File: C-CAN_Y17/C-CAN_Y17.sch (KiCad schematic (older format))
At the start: 10 parts

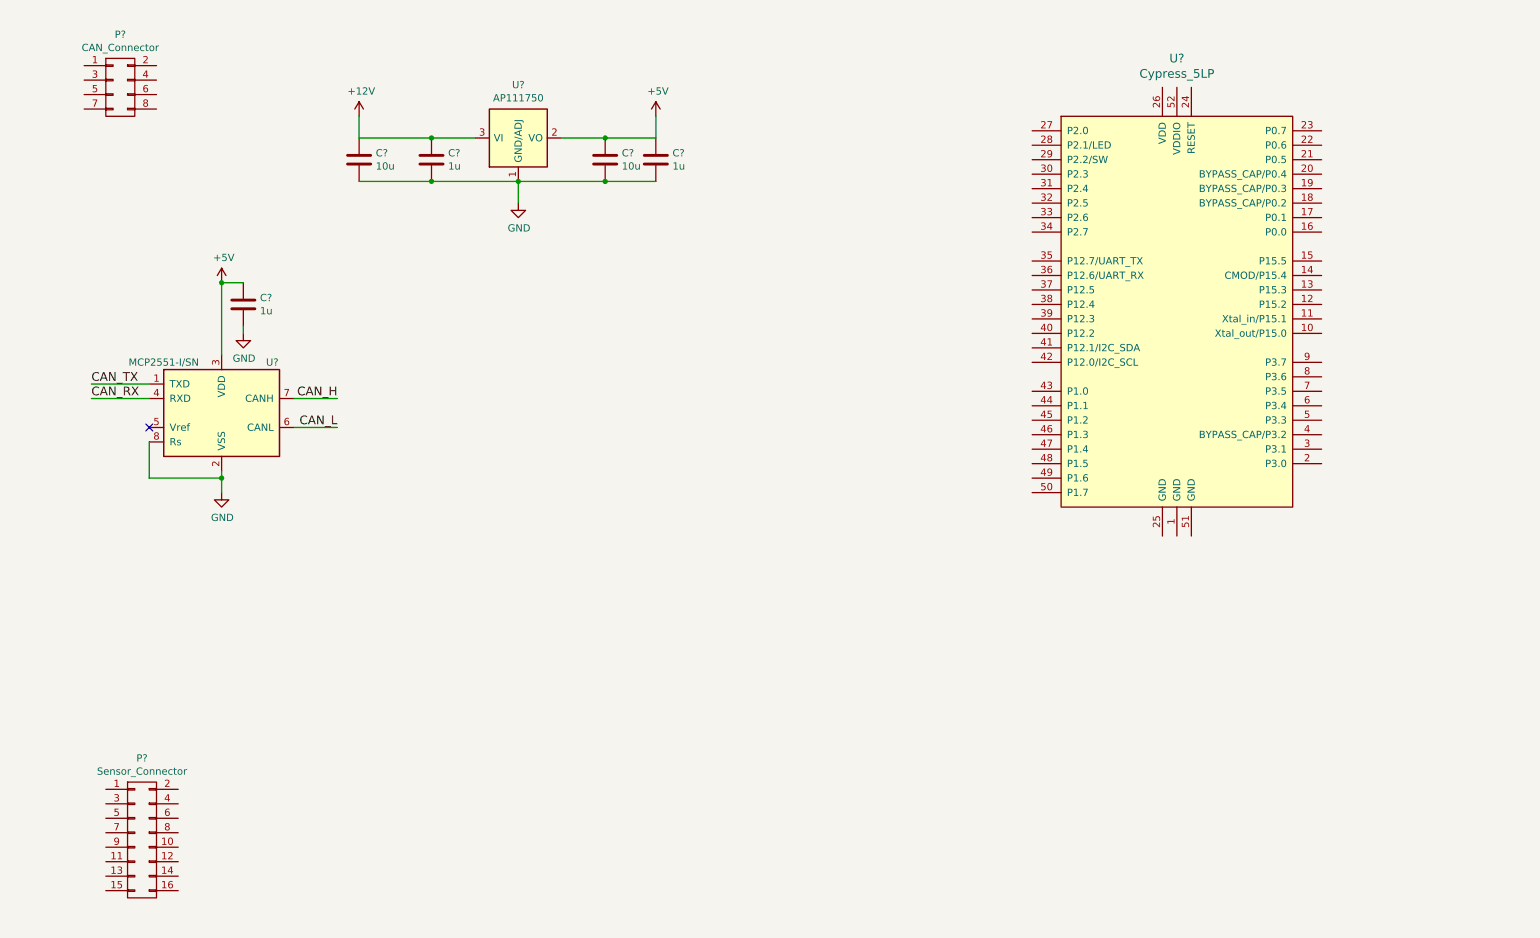
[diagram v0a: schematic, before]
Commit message: More work on new C-CAN
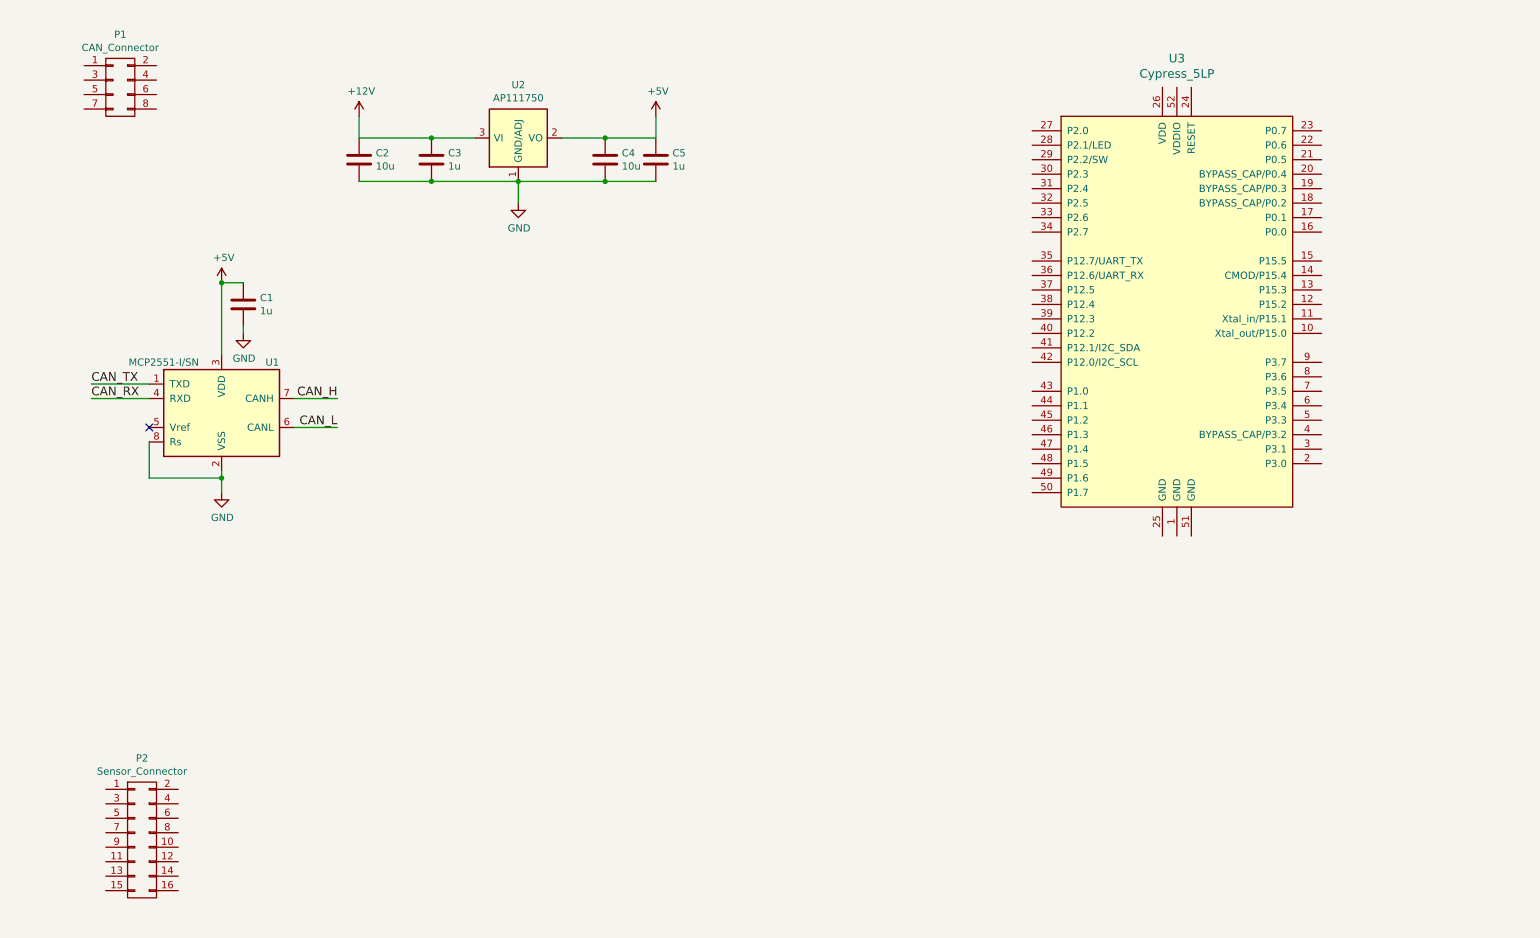
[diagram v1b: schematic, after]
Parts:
- P2: renamed from P?; footprint (none) -> UNCAMotorsports:MX150_16pin
- gave numbers to parts that had none: 9
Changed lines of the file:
@@
 LIBS:contrib
 LIBS:valves
+LIBS:Cypress_cy8c5xlp
 LIBS:UNCAMotorsports
-LIBS:Cypress_cy8c5xlp
+LIBS:relays
+LIBS:SystemBlocks
+LIBS:C-CAN_Y17-cache
 EELAYER 26 0
 EELAYER END
@@
 $EndDescr
 $Comp
-L Cypress_5LP U?
+L Cypress_5LP U3
 U 1 1 58B77315
 P 8800 2600
-F 0 "U?" H 8800 4300 60  0000 C CNN
+F 0 "U3" H 8800 4300 60  0000 C CNN
 F 1 "Cypress_5LP" H 8800 4194 60  0000 C CNN
-F 2 "" H 8800 2800 60  0000 C CNN
+F 2 "" H 8800 2800 60  0001 C CNN
 F 3 "" H 8800 2800 60  0000 C CNN
 	1    8800 2600
@@
 $EndComp
 $Comp
-L MCP2551-I/SN U?
+L MCP2551-I/SN U1
 U 1 1 58B7735B
 P 2200 3350
-F 0 "U?" H 2550 3700 50  0000 C CNN
+F 0 "U1" H 2550 3700 50  0000 C CNN
 F 1 "MCP2551-I/SN" H 1800 3700 50  0000 C CNN
 F 2 "Housings_SOIC:SOIC-8_3.9x4.9mm_Pitch1.27mm" H 2200 2850 50  0001 C CIN
@@
 $EndComp
 $Comp
-L AP111750 U?
+L AP111750 U2
 U 1 1 58B7742F
 P 4250 1450
-F 0 "U?" H 4250 1817 50  0000 C CNN
+F 0 "U2" H 4250 1817 50  0000 C CNN
 F 1 "AP111750" H 4250 1726 50  0000 C CNN
 F 2 "TO_SOT_Packages_SMD:SOT-223" H 4250 1100 50  0001 C CNN
@@
 $EndComp
 $Comp
-L CONN_02X04 P?
+L CONN_02X04 P1
 U 1 1 58B775B9
 P 1500 1100
-F 0 "P?" H 1500 1465 50  0000 C CNN
+F 0 "P1" H 1500 1465 50  0000 C CNN
 F 1 "CAN_Connector" H 1500 1374 50  0000 C CNN
-F 2 "" H 1500 -100 50  0000 C CNN
+F 2 "" H 1500 -100 50  0001 C CNN
 F 3 "" H 1500 -100 50  0000 C CNN
 	1    1500 1100
@@
 $EndComp
 $Comp
-L CONN_02X08 P?
+L CONN_02X08 P2
 U 1 1 58B77DCE
 P 1650 6300
-F 0 "P?" H 1650 6865 50  0000 C CNN
+F 0 "P2" H 1650 6865 50  0000 C CNN
 F 1 "Sensor_Connector" H 1650 6774 50  0000 C CNN
-F 2 "" H 1650 5100 50  0000 C CNN
+F 2 "UNCAMotorsports:MX150_16pin" H 1650 5100 50  0001 C CNN
 F 3 "" H 1650 5100 50  0000 C CNN
 	1    1650 6300
@@
 $EndComp
 $Comp
-L +12V #PWR?
+L +12V #PWR01
 U 1 1 58B77F9E
 P 3150 1300
-F 0 "#PWR?" H 3150 1150 50  0001 C CNN
+F 0 "#PWR01" H 3150 1150 50  0001 C CNN
 F 1 "+12V" H 3165 1473 50  0000 C CNN
 F 2 "" H 3150 1300 50  0000 C CNN
@@
 $EndComp
 $Comp
-L +5V #PWR?
+L +5V #PWR02
 U 1 1 58B77FBC
 P 5200 1300
-F 0 "#PWR?" H 5200 1150 50  0001 C CNN
+F 0 "#PWR02" H 5200 1150 50  0001 C CNN
 F 1 "+5V" H 5215 1473 50  0000 C CNN
 F 2 "" H 5200 1300 50  0000 C CNN
@@
 $EndComp
 $Comp
-L C C?
+L C C2
 U 1 1 58B77FDA
 P 3150 1600
-F 0 "C?" H 3265 1646 50  0000 L CNN
+F 0 "C2" H 3265 1646 50  0000 L CNN
 F 1 "10u" H 3265 1555 50  0000 L CNN
-F 2 "" H 3188 1450 50  0000 C CNN
+F 2 "" H 3188 1450 50  0001 C CNN
 F 3 "" H 3150 1600 50  0000 C CNN
 	1    3150 1600
@@
 $EndComp
 $Comp
-L C C?
+L C C3
 U 1 1 58B78024
 P 3650 1600
-F 0 "C?" H 3765 1646 50  0000 L CNN
+F 0 "C3" H 3765 1646 50  0000 L CNN
 F 1 "1u" H 3765 1555 50  0000 L CNN
-F 2 "" H 3688 1450 50  0000 C CNN
+F 2 "" H 3688 1450 50  0001 C CNN
 F 3 "" H 3650 1600 50  0000 C CNN
 	1    3650 1600
@@
 $EndComp
 $Comp
-L C C?
+L C C4
 U 1 1 58B7804C
 P 4850 1600
-F 0 "C?" H 4965 1646 50  0000 L CNN
+F 0 "C4" H 4965 1646 50  0000 L CNN
 F 1 "10u" H 4965 1555 50  0000 L CNN
-F 2 "" H 4888 1450 50  0000 C CNN
+F 2 "" H 4888 1450 50  0001 C CNN
 F 3 "" H 4850 1600 50  0000 C CNN
 	1    4850 1600
@@
 $EndComp
 $Comp
-L C C?
+L C C5
 U 1 1 58B7807E
 P 5200 1600
-F 0 "C?" H 5315 1646 50  0000 L CNN
+F 0 "C5" H 5315 1646 50  0000 L CNN
 F 1 "1u" H 5315 1555 50  0000 L CNN
-F 2 "" H 5238 1450 50  0000 C CNN
+F 2 "" H 5238 1450 50  0001 C CNN
 F 3 "" H 5200 1600 50  0000 C CNN
 	1    5200 1600
@@
 	5200 1450 5200 1300
 $Comp
-L GND #PWR?
+L GND #PWR03
 U 1 1 58B78147
 P 4250 1900
-F 0 "#PWR?" H 4250 1650 50  0001 C CNN
+F 0 "#PWR03" H 4250 1650 50  0001 C CNN
 F 1 "GND" H 4255 1727 50  0000 C CNN
 F 2 "" H 4250 1900 50  0000 C CNN
@@
 Connection ~ 4850 1750
 $Comp
-L GND #PWR?
+L GND #PWR04
 U 1 1 58B78482
 P 2200 3900
-F 0 "#PWR?" H 2200 3650 50  0001 C CNN
+F 0 "#PWR04" H 2200 3650 50  0001 C CNN
 F 1 "GND" H 2205 3727 50  0000 C CNN
 F 2 "" H 2200 3900 50  0000 C CNN
@@
 	2700 3450 3000 3450
 $Comp
-L +5V #PWR?
+L +5V #PWR05
 U 1 1 58B786DB
 P 2200 2450
-F 0 "#PWR?" H 2200 2300 50  0001 C CNN
+F 0 "#PWR05" H 2200 2300 50  0001 C CNN
 F 1 "+5V" H 2215 2623 50  0000 C CNN
 F 2 "" H 2200 2450 50  0000 C CNN
@@
 	2200 2450 2200 2950
 $Comp
-L C C?
+L C C1
 U 1 1 58B78755
 P 2350 2600
-F 0 "C?" H 2465 2646 50  0000 L CNN
+F 0 "C1" H 2465 2646 50  0000 L CNN
 F 1 "1u" H 2465 2555 50  0000 L CNN
-F 2 "" H 2388 2450 50  0000 C CNN
+F 2 "" H 2388 2450 50  0001 C CNN
 F 3 "" H 2350 2600 50  0000 C CNN
 	1    2350 2600
@@
 $EndComp
 $Comp
-L GND #PWR?
+L GND #PWR06
 U 1 1 58B7879B
 P 2350 2800
-F 0 "#PWR?" H 2350 2550 50  0001 C CNN
+F 0 "#PWR06" H 2350 2550 50  0001 C CNN
 F 1 "GND" H 2355 2627 50  0000 C CNN
 F 2 "" H 2350 2800 50  0000 C CNN

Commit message: "        "
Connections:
- net +12V: now also P1.1 (P1), P1.4 (P4)
- net +5V: now also P2.1 (P1), P2.4 (P4), P2.7 (P7), P2.9 (P9)
- net CAN_H: now also P1.2 (P2), P1.3 (P3)
- net CAN_L: now also P1.6 (P6), P1.7 (P7)
- net GND: now also P1.5 (P5), P1.8 (P8), P2.3 (P3), P2.6 (P6)
- net S1: now reaches P2.2 (P2)
- net S2: now reaches P2.5 (P5)
- net H1: now reaches P2.8 (P8)
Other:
- moved on the sheet: P2
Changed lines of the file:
@@
 U 1 1 58B77315
 P 8800 2600
-F 0 "U3" H 8800 4300 60  0000 C CNN
-F 1 "Cypress_5LP" H 8800 4194 60  0000 C CNN
+F 0 "U3" H 8250 4050 60  0000 C CNN
+F 1 "Cypress_5LP" H 8300 3950 60  0000 C CNN
 F 2 "" H 8800 2800 60  0001 C CNN
 F 3 "" H 8800 2800 60  0000 C CNN
@@
 L CONN_02X08 P2
 U 1 1 58B77DCE
-P 1650 6300
-F 0 "P2" H 1650 6865 50  0000 C CNN
-F 1 "Sensor_Connector" H 1650 6774 50  0000 C CNN
-F 2 "UNCAMotorsports:MX150_16pin" H 1650 5100 50  0001 C CNN
-F 3 "" H 1650 5100 50  0000 C CNN
-	1    1650 6300
+P 3400 5350
+F 0 "P2" H 3400 5915 50  0000 C CNN
+F 1 "Sensor_Connector" H 3400 5824 50  0000 C CNN
+F 2 "UNCAMotorsports:MX150_16pin" H 3400 4150 50  0001 C CNN
+F 3 "" H 3400 4150 50  0000 C CNN
+	1    3400 5350
 	1    0    0    -1
 $EndComp
@@
 	2350 2450 2200 2450
 Connection ~ 2200 2450
+Text Label 950  1050 0    60   ~ 0
+CAN_H
+Text Label 2100 950  2    60   ~ 0
+CAN_H
+Wire Wire Line
+	2100 950  1750 950
+$Comp
+L +12V #PWR?
+U 1 1 58B7A343
+P 850 950
+F 0 "#PWR?" H 850 800 50  0001 C CNN
+F 1 "+12V" H 865 1123 50  0000 C CNN
+F 2 "" H 850 950 50  0000 C CNN
+F 3 "" H 850 950 50  0000 C CNN
+	1    850  950
+	1    0    0    -1
+$EndComp
+Wire Wire Line
+	850  950  1250 950
+$Comp
+L +12V #PWR?
+U 1 1 58B7A390
+P 2200 1050
+F 0 "#PWR?" H 2200 900 50  0001 C CNN
+F 1 "+12V" H 2215 1223 50  0000 C CNN
+F 2 "" H 2200 1050 50  0000 C CNN
+F 3 "" H 2200 1050 50  0000 C CNN
+	1    2200 1050
+	1    0    0    -1
+$EndComp
+Wire Wire Line
+	2200 1050 1750 1050
+$Comp
+L GND #PWR?
+U 1 1 58B7A3DE
+P 850 1150
+F 0 "#PWR?" H 850 900 50  0001 C CNN
+F 1 "GND" H 855 977 50  0000 C CNN
+F 2 "" H 850 1150 50  0000 C CNN
+F 3 "" H 850 1150 50  0000 C CNN
+	1    850  1150
+	1    0    0    -1
+$EndComp
+Wire Wire Line
+	850  1150 1250 1150
+$Comp
+L GND #PWR?
+U 1 1 58B7A438
+P 2200 1250
+F 0 "#PWR?" H 2200 1000 50  0001 C CNN
+F 1 "GND" H 2205 1077 50  0000 C CNN
+F 2 "" H 2200 1250 50  0000 C CNN
+F 3 "" H 2200 1250 50  0000 C CNN
+	1    2200 1250
+	1    0    0    -1
+$EndComp
+Wire Wire Line
+	2200 1250 1750 1250
+Text Label 2100 1150 2    60   ~ 0
+CAN_L
+Wire Wire Line
+	2100 1150 1750 1150
+Text Label 950  1250 0    60   ~ 0
+CAN_L
+Wire Wire Line
+	950  1250 1250 1250
+Wire Wire Line
+	950  1050 1250 1050
+$Comp
+L +5V #PWR?
+U 1 1 58B7AF23
+P 2700 5000
+F 0 "#PWR?" H 2700 4850 50  0001 C CNN
+F 1 "+5V" H 2715 5173 50  0000 C CNN
+F 2 "" H 2700 5000 50  0000 C CNN
+F 3 "" H 2700 5000 50  0000 C CNN
+	1    2700 5000
+	1    0    0    -1
+$EndComp
+Wire Wire Line
+	2700 5000 3150 5000
+Text Label 3900 5000 2    60   ~ 0
+S1
+Wire Wire Line
+	3900 5000 3650 5000
+$Comp
+L GND #PWR?
+U 1 1 58B7B062
+P 2700 5100
+F 0 "#PWR?" H 2700 4850 50  0001 C CNN
+F 1 "GND" H 2705 4927 50  0000 C CNN
+F 2 "" H 2700 5100 50  0000 C CNN
+F 3 "" H 2700 5100 50  0000 C CNN
+	1    2700 5100
+	1    0    0    -1
+$EndComp
+Wire Wire Line
+	2700 5100 3150 5100
+$Comp
+L +5V #PWR?
+U 1 1 58B7B0B7
+P 4200 5100
+F 0 "#PWR?" H 4200 4950 50  0001 C CNN
+F 1 "+5V" H 4215 5273 50  0000 C CNN
+F 2 "" H 4200 5100 50  0000 C CNN
+F 3 "" H 4200 5100 50  0000 C CNN
+	1    4200 5100
+	1    0    0    -1
+$EndComp
+Wire Wire Line
+	4200 5100 3650 5100
+Text Label 3000 5200 0    60   ~ 0
+S2
+Wire Wire Line
+	3000 5200 3150 5200
+$Comp
+L GND #PWR?
+U 1 1 58B7B15B
+P 4200 5200
+F 0 "#PWR?" H 4200 4950 50  0001 C CNN
+F 1 "GND" H 4205 5027 50  0000 C CNN
+F 2 "" H 4200 5200 50  0000 C CNN
+F 3 "" H 4200 5200 50  0000 C CNN
+	1    4200 5200
+	1    0    0    -1
+$EndComp
+Wire Wire Line
+	4200 5200 3650 5200
+$Comp
+L +5V #PWR?
+U 1 1 58B7B1B3
+P 2500 5300
+F 0 "#PWR?" H 2500 5150 50  0001 C CNN
+F 1 "+5V" H 2515 5473 50  0000 C CNN
+F 2 "" H 2500 5300 50  0000 C CNN
+F 3 "" H 2500 5300 50  0000 C CNN
+	1    2500 5300
+	1    0    0    -1
+$EndComp
+Wire Wire Line
+	2500 5300 3150 5300
+Text Label 3900 5300 2    60   ~ 0
+H1
+Wire Wire Line
+	3900 5300 3650 5300
+Wire Wire Line
+	3150 5400 2500 5400
+Wire Wire Line
+	2500 5400 2500 5300
+Connection ~ 2500 5300
 $EndSCHEMATC

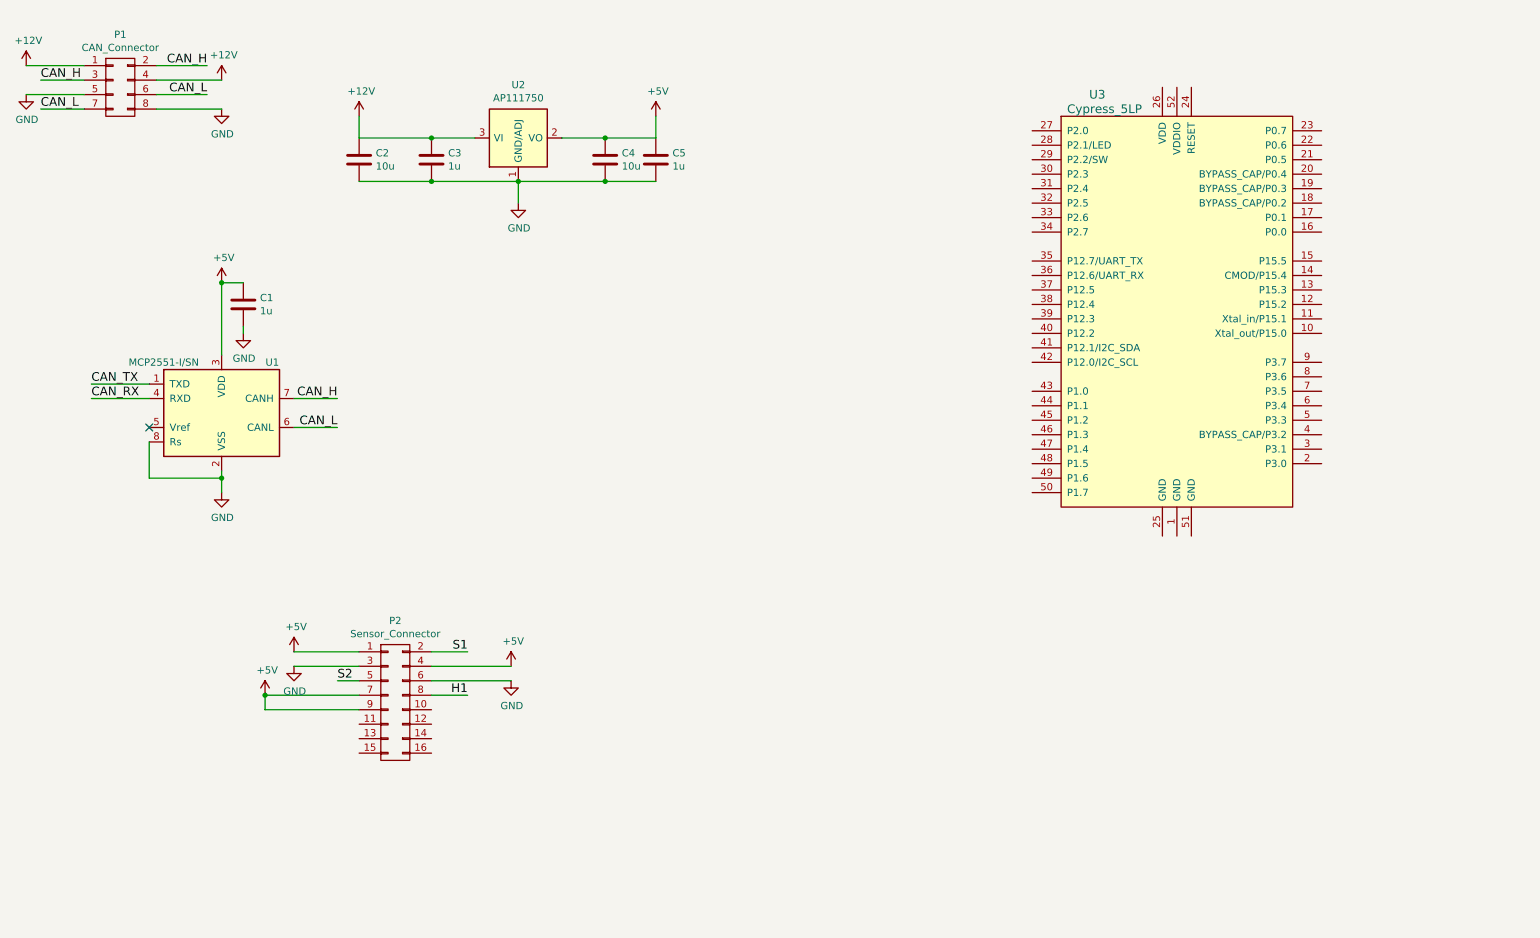
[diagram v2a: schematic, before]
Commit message: C-CAN_Y17 done except for pcb
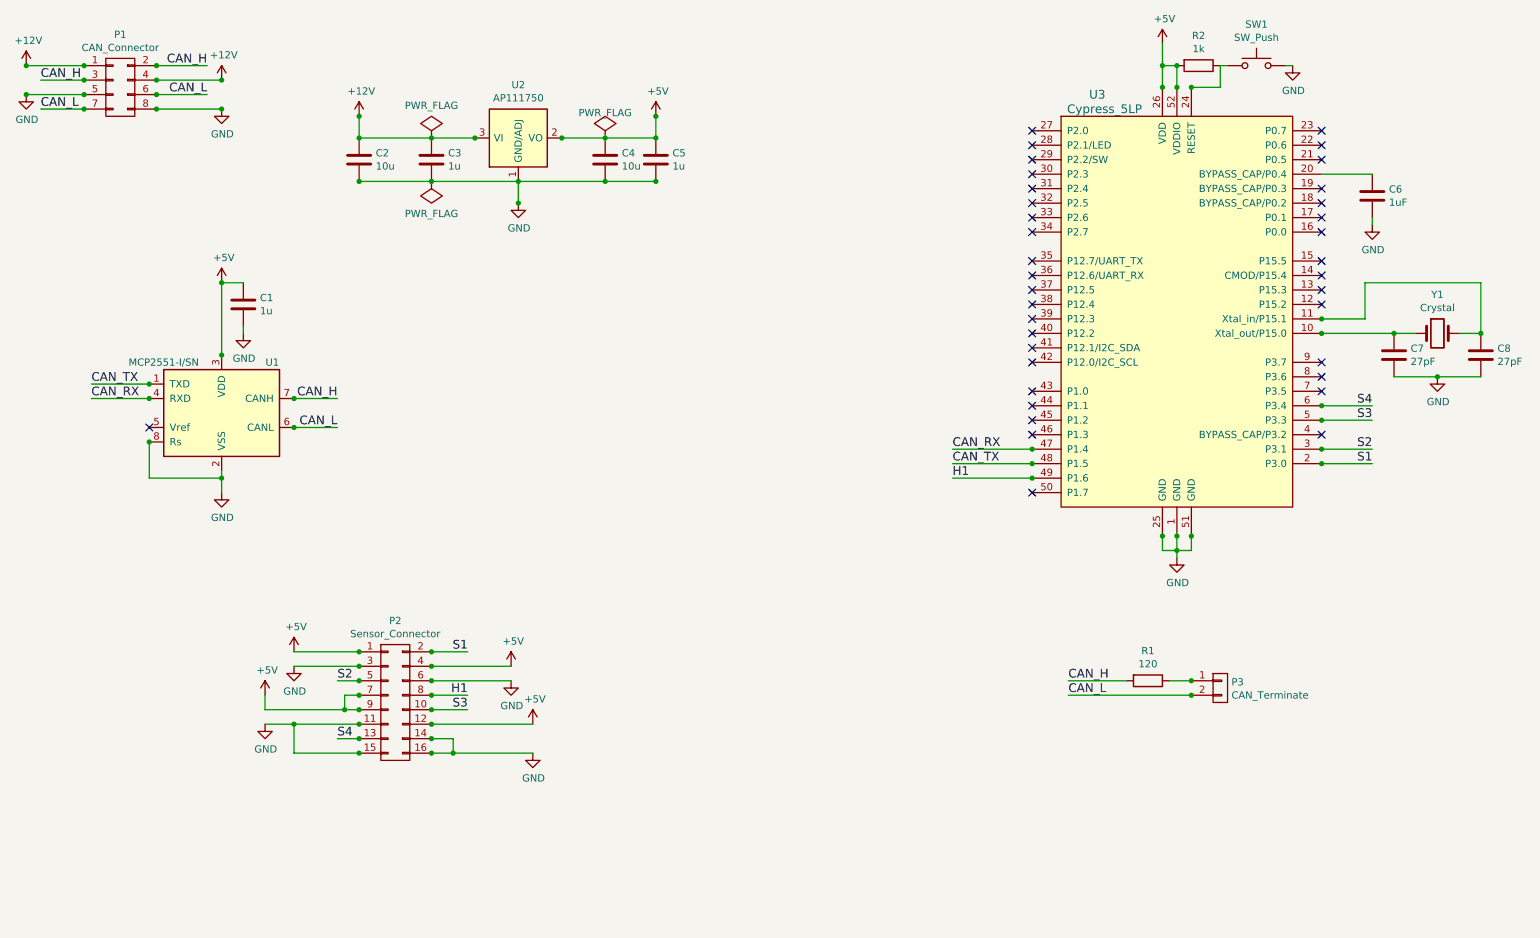
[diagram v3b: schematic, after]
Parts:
- added C6: 1uF, Capacitors_SMD:C_0805_HandSoldering, symbol C
- added C7, C8: 27pF, Capacitors_SMD:C_0805_HandSoldering, symbol C
- added P3: CAN_Terminate, Pin_Headers:Pin_Header_Straight_1x02_Pitch2.54mm, symbol CONN_01X02
- added R1: 120, Resistors_SMD:R_0805_HandSoldering, symbol R
- added R2: 1k, Resistors_SMD:R_0805_HandSoldering, symbol R
- added SW1: SW_Push, Buttons_Switches_ThroughHole:SW_PUSH_6mm, symbol SW_Push
- added Y1: Crystal, Crystals:Crystal_SMD_HC49-SD_HandSoldering, symbol Crystal
- C1, C2, C3, C4, C5: footprint (none) -> Capacitors_SMD:C_0805_HandSoldering
- P1: footprint (none) -> UNCAMotorsports:MX150_8Pin
- U3: footprint (none) -> UNCAMotorsports:CypressPSoC
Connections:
- net +5V: now also P2.12 (P12), U3.26 (VDD), U3.52 (VDDIO), R2.2
- net CAN_H: now also R1.2
- net CAN_L: now also P3.2 (P2)
- net CAN_RX: now also U3.47 (P1.4)
- net CAN_TX: now also U3.48 (P1.5)
- net GND: now also P2.11 (P11), P2.14 (P14), P2.15 (P15), P2.16 (P16), U3.1 (GND), U3.25 (GND), U3.51 (GND), C6.2, C7.2, C8.2, SW1.2
- net H1: now also U3.49 (P1.6)
- net S1: now also U3.2 (P3.0)
- net S2: now also U3.3 (P3.1)
- net at U3.10 (Xtal_out/P15.0): now also C7.1, Y1.1
- net at U3.11 (Xtal_in/P15.1): now also C8.1, Y1.2
- net at U3.20 (BYPASS_CAP/P0.4): now also C6.1
- net at U3.24 (RESET): now also R2.1, SW1.1
- net S3: now reaches U3.5 (P3.3)
- net S3: now also P2.10 (P10)
- net S4: now reaches U3.6 (P3.4)
- net S4: now also P2.13 (P13)
- new net: P3.1 (P1), R1.1
- no-connect marks 1 -> 37
